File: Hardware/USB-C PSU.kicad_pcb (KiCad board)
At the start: 8 copper layers, 50 x 50 mm, 147 parts, among them J1 USB_C_Receptacle_USB2.0_16P, J101 USB_C_Receptacle_USB2.0_16P, J102 ST7789 LCD, J103 TC2030, J104 Expansion, J2 VOUT, J3 TC2030, J4 VIN, Q1 100V 50A, Q101 AO3400A, Q2 100V 50A, Q3 100V 50A, Q4 100V 50A, SW1 SW_Reverse, SW101 SIQ-02FVS3, SW102 SW_Back, SW103 Reset, SW104 Boot, SW2 Boot, SW3 Reset, U1 CH32X035G8U6, U101 CH32X035G8U6, U102 AP2112K-3.3, U103 TPS22915CYFPR, U104 SIT3088ETK, U105 LIS3DH, U2 BQ25758A, U4 LMR51610XDBVR, U5 TPD4S480RUKR, U6 TPS22915CYFPR, U7 TPS22915CYFPR

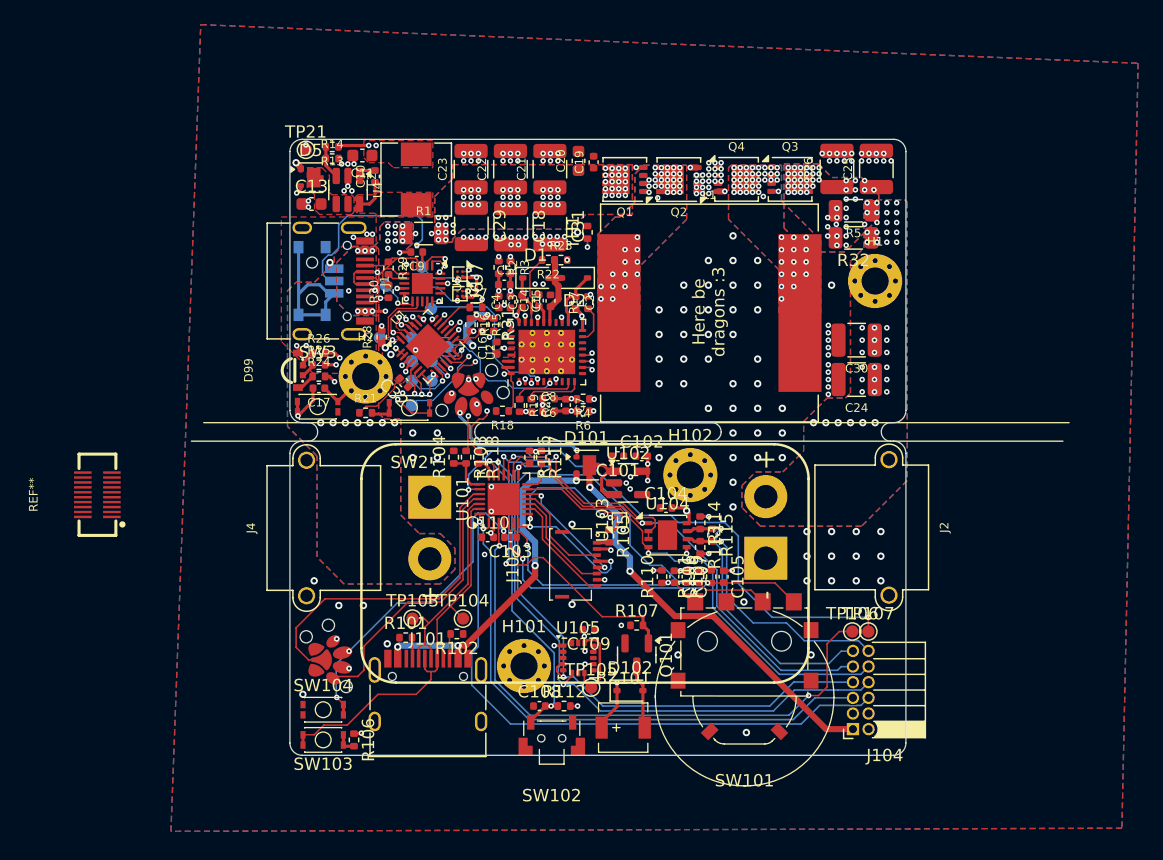
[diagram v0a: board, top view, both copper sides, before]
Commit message: design silkscreen markings + some polish
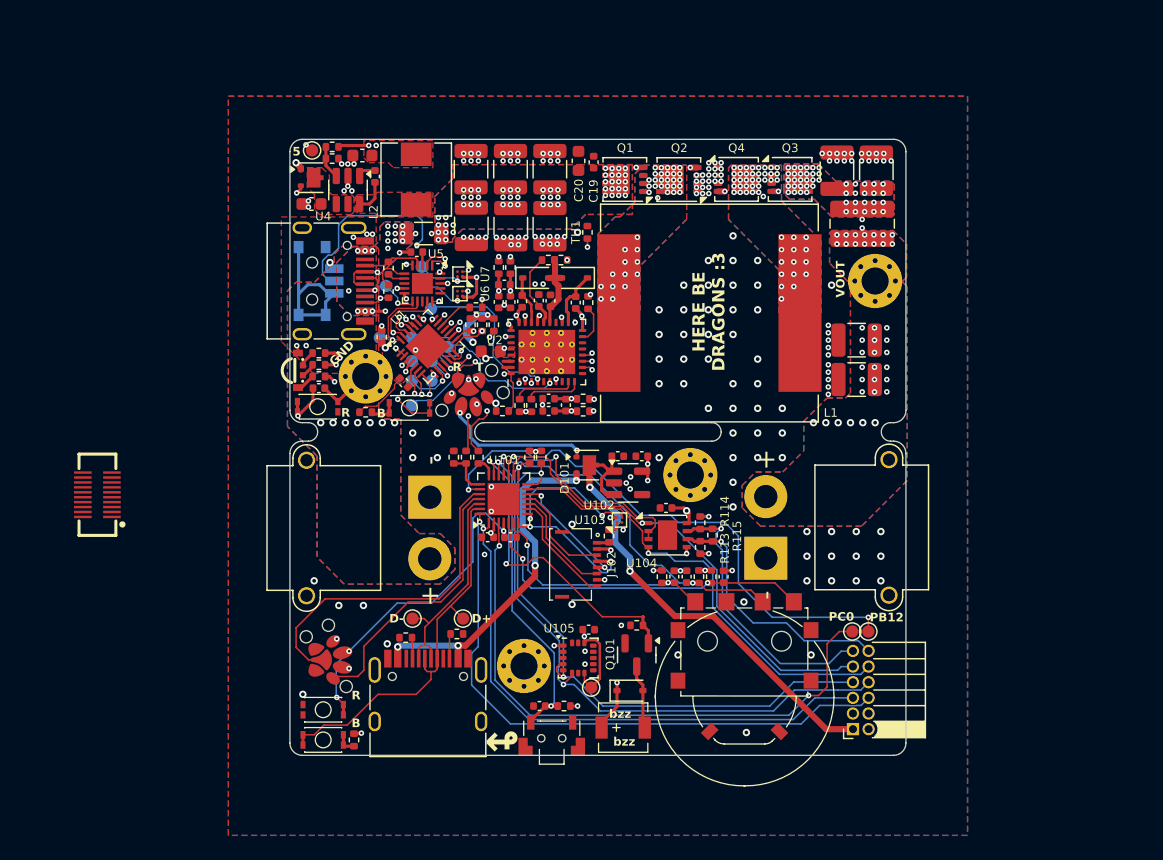
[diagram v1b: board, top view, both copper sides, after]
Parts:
- removed R32: 10m, Resistor_SMD:R_1206_3216Metric
- added ?: , clipboard:e777734a-e85c-4367-9ebd-f48524917f5c, B.Cu at (117.6, 76.7)
- added G***: LOGO, LeoDJ-kicad:Logo_PCBDerg_Mask_10mm, B.Cu at (134.4, 92.8)
- added REF**: OSHW-Symbol_6.7x6mm_SilkScreen, Symbol:OSHW-Symbol_6.7x6mm_SilkScreen, B.Cu at (146.6, 97.3)
- added kibuzzard-67A54591: G***, kibuzzard-67A54591, B.Cu at (106.8, 78.9)
- C14: value 4u7u 25V -> 4u7 25V
- C16: footprint Capacitor_SMD:C_0402_1005Metric -> Capacitor_SMD:C_0603_1608Metric
- R5: value 10m -> 5m; footprint Resistor_SMD:R_1206_3216Metric -> Resistor_SMD:R_1020_2550Metric_Pad1.33x5.20mm_HandSolder
- moved R5 1.26 mm to (146.8, 84.5), turned to 90 degrees
- moved C16 0.57 mm to (116.7, 94.9), turned to 180 degrees
- moved TP21 0.50 mm to (102.2, 78.6)
- moved C25 0.15 mm to (148.0, 80.2)
- moved C26 0.15 mm to (144.8, 80.2)
- moved R21 0.05 mm to (106.5, 99.8)
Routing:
- net VOUT: track 110.9 -> 118.4 mm, vias 47 -> 42
- net CAP_VOUT: track 29.2 -> 31.7 mm, vias 50 -> 49
- net +5V: track 95.4 -> 95.3 mm, vias 15 -> 14
- net GND: vias 191 -> 193
- added copper zone on In2.Cu, net CAP_VOUT
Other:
- board text added: "5"
- board text added: "A PB0 SDA C14 GND 3V3"
- board text added: "A3"
- board text added: "A4"
- board text added: "A5"
- board text added: "A6"
- board text added: "A7"
- board text added: "B"
- board text added: "B PB5 SCL PC15 GND 5V"
- board text added: "CC1"
- board text added: "CC2"
- board text added: "D+"
- board text added: "D-"
- board text added: "EN"
- board text added: "GND"
- board text added: "HERE BE DRAGONS :3"
- board text added: "INT"
- board text added: "PB12"
- board text added: "PC0"
- board text added: "PG"
- board text added: "R"
- board text added: "R B"
- board text added: "STAT"
- board text added: "T"
- board text added: "V1EN"
- board text added: "V2EN"
- board text added: "VOUT"
- board text added: "by LeoDJ"
- board text added: "bzz bzz"
- board text added: "https://github.com/ LeoDJ/USB-C_PD_PSU"
- board text added: "v1.0"
- board text added: "↫"
- board text removed: "Here be dragons :3"

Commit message: final tweaks for v1.0
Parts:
- removed the REF** at (84.8, 106.5)
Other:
- board text added: "1"
- board text added: "2"
- board text added: "3"
- board text added: "4"
- board text added: "6"
- board text added: "F"
